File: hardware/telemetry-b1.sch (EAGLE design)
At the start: 128 parts, among them IC1 COPERNICUSSMD, IC10 TPS70933, IC2 TPS70933, IC4 STM32L073CZT6, IC5 TPS62160, IC6 HX1, IC7 LMP7702, IC9 HIH9131, J1 I2C1, J10 TEMP_BAT, J11 DNP, J12 INSOL, J13 SMA_EDGE, J2 I2C2, J3 SMA_EDGE, J4 USD-SOCKET, J5 BAT, J6 SMA_EDGE, J7 SMA_EDGE, J8 TEMP_GPS, J9 TEMP_HOT, K1 ARE104H, K2 ARE104H, K3 ARE104H, Q1 AO3400A, Q2 AO3400A, Q3 AO3400A, U1 LTC3105, U2 INA219, Y1 32768, Y2 8M

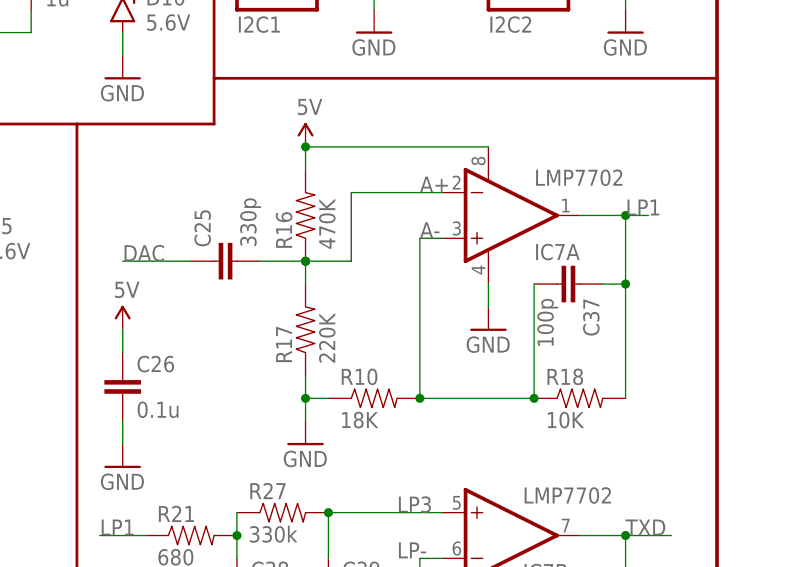
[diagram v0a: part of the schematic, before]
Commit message: Fixed swapped pins in DAC filter
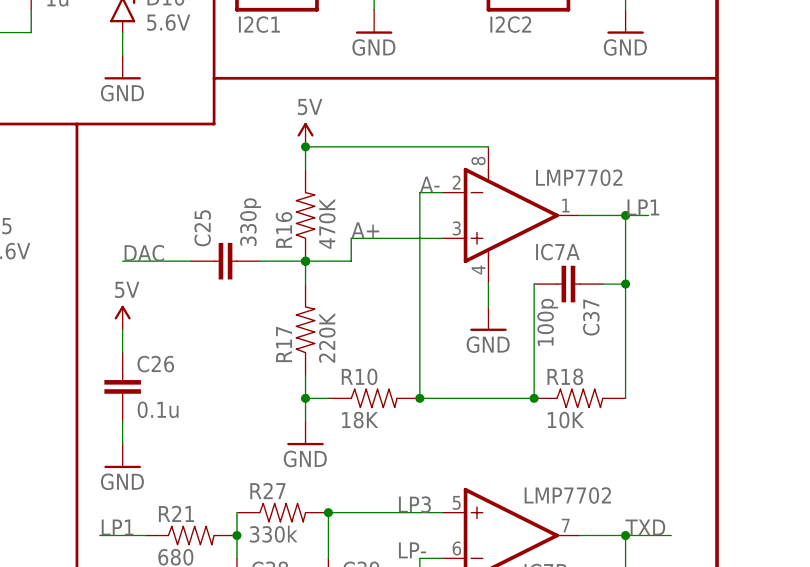
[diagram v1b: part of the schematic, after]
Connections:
- net A+: now also IC7A.+IN; no longer IC7A.-IN
- net A-: now also IC7A.-IN; no longer IC7A.+IN
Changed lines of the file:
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@@
 <net name="A-" class="0">
 <segment>
-<wire x1="215.9" y1="139.7" x2="215.9" y2="121.92" width="0.1524" layer="91"/>
-<label x="215.9" y="139.7" size="1.778" layer="95"/>
-<pinref part="IC7" gate="A" pin="+IN"/>
-<wire x1="218.44" y1="139.7" x2="215.9" y2="139.7" width="0.1524" layer="91"/>
+<wire x1="215.9" y1="144.78" x2="215.9" y2="121.92" width="0.1524" layer="91"/>
 <pinref part="R10" gate="G$1" pin="2"/>
 <pinref part="C37" gate="G$1" pin="2"/>
@@
 <junction x="228.6" y="121.92"/>
 <junction x="215.9" y="121.92"/>
+<pinref part="IC7" gate="A" pin="-IN"/>
+<wire x1="215.9" y1="144.78" x2="218.44" y2="144.78" width="0.1524" layer="91"/>
+<label x="215.9" y="144.78" size="1.778" layer="95"/>
 </segment>
 </net>
@@
 <junction x="203.2" y="137.16"/>
 <junction x="203.2" y="137.16"/>
-<label x="215.9" y="144.78" size="1.778" layer="95"/>
-<wire x1="208.28" y1="144.78" x2="208.28" y2="137.16" width="0.1524" layer="91"/>
+<wire x1="208.28" y1="139.7" x2="208.28" y2="137.16" width="0.1524" layer="91"/>
 <wire x1="208.28" y1="137.16" x2="203.2" y2="137.16" width="0.1524" layer="91"/>
-<pinref part="IC7" gate="A" pin="-IN"/>
-<wire x1="218.44" y1="144.78" x2="208.28" y2="144.78" width="0.1524" layer="91"/>
+<pinref part="IC7" gate="A" pin="+IN"/>
+<wire x1="218.44" y1="139.7" x2="208.28" y2="139.7" width="0.1524" layer="91"/>
+<label x="208.28" y="139.7" size="1.778" layer="95"/>
 </segment>
 </net>

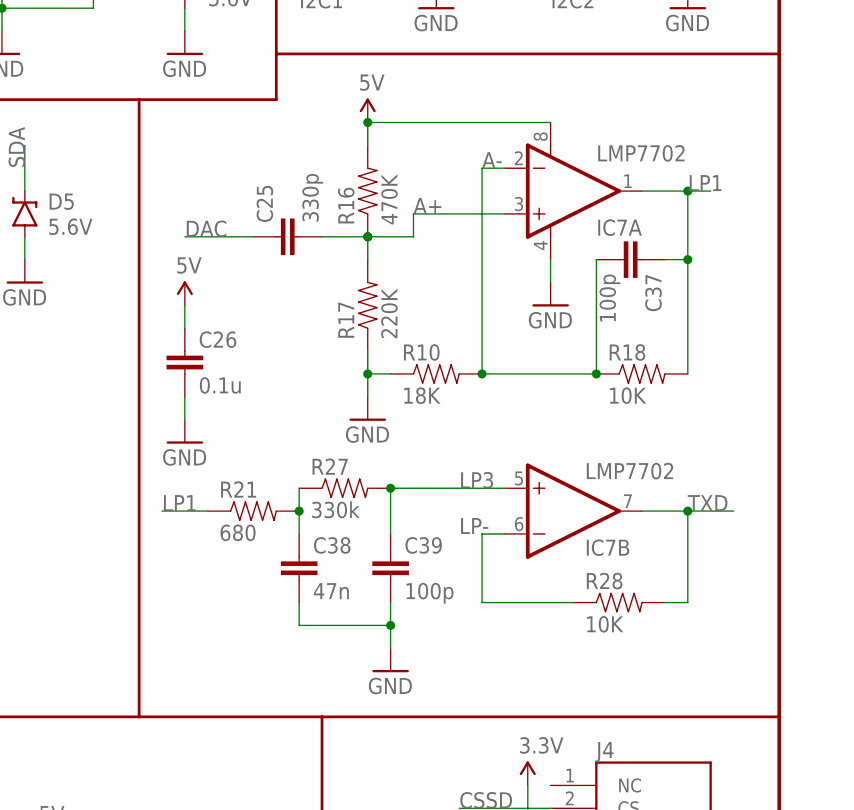
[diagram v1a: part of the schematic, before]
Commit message: Copy filter changes from main Telemetry PCB. Needs a relay rework.
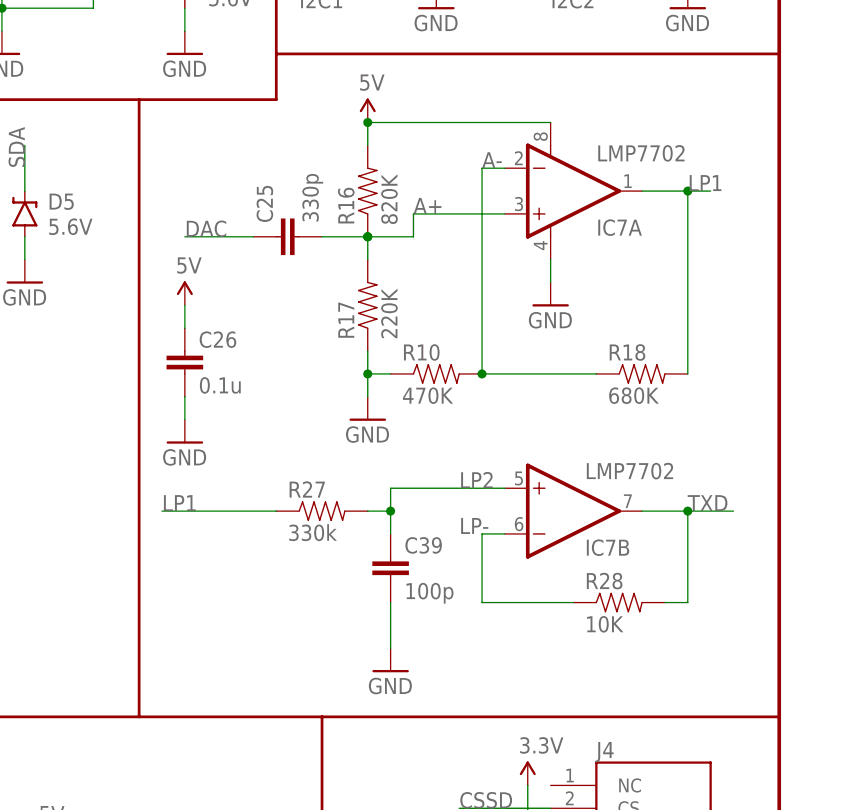
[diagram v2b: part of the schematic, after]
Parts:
- removed C37: 100p, SparkFun-Passives:CAP0805
- removed C38: 47n, SparkFun-Passives:CAP0805
- removed R21: 680, SparkFun-Passives:RESISTOR0805-RES
- R10: value 18K -> 470K
- R16: value 470K -> 820K
- R18: value 10K -> 680K
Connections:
- removed net LP3: C39.1, IC7B.+IN, R27.2
- net A-: no longer C37.2
- net GND: no longer C38.2
- net LP1: now also R27.1; no longer C37.1, R21.1
- net LP2: now also C39.1, IC7B.+IN, R27.2; no longer C38.1, R21.2, R27.1
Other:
- moved on the sheet: R27
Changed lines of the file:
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@@
 <part name="GND25" library="SparkFun-Aesthetics" deviceset="GND" device=""/>
 <part name="C25" library="SparkFun-Passives" deviceset="CAP" device="0805" value="330p"/>
-<part name="R16" library="SparkFun-Passives" deviceset="RESISTOR" device="0805-RES" value="470K"/>
+<part name="R16" library="SparkFun-Passives" deviceset="RESISTOR" device="0805-RES" value="820K"/>
 <part name="R17" library="SparkFun-Passives" deviceset="RESISTOR" device="0805-RES" value="220K"/>
-<part name="R18" library="SparkFun-Passives" deviceset="RESISTOR" device="0805-RES" value="10K"/>
+<part name="R18" library="SparkFun-Passives" deviceset="RESISTOR" device="0805-RES" value="680K"/>
 <part name="C26" library="SparkFun-Passives" deviceset="CAP" device="0805" value="0.1u"/>
 <part name="GND26" library="SparkFun-Aesthetics" deviceset="GND" device=""/>
@@
 <part name="GND48" library="SparkFun-Aesthetics" deviceset="GND" device=""/>
 <part name="SUPPLY20" library="SparkFun-Aesthetics" deviceset="3.3V" device=""/>
-<part name="C37" library="SparkFun-Passives" deviceset="CAP" device="0805" value="100p"/>
-<part name="R10" library="SparkFun-Passives" deviceset="RESISTOR" device="0805-RES" value="18K"/>
-<part name="R21" library="SparkFun-Passives" deviceset="RESISTOR" device="0805-RES" value="680"/>
-<part name="C38" library="SparkFun-Passives" deviceset="CAP" device="0805" value="47n"/>
+<part name="R10" library="SparkFun-Passives" deviceset="RESISTOR" device="0805-RES" value="470K"/>
 <part name="SUPPLY25" library="SparkFun-Aesthetics" deviceset="5V" device=""/>
 <part name="R27" library="SparkFun-Passives" deviceset="RESISTOR" device="0805-RES" value="330k"/>
@@
 <instance part="GND48" gate="1" x="182.88" y="157.48"/>
 <instance part="SUPPLY20" gate="G$1" x="182.88" y="170.18"/>
-<instance part="C37" gate="G$1" x="231.14" y="134.62" rot="R270"/>
 <instance part="R10" gate="G$1" x="210.82" y="121.92"/>
-<instance part="R21" gate="G$1" x="190.5" y="106.68"/>
-<instance part="C38" gate="G$1" x="195.58" y="99.06"/>
 <instance part="SUPPLY25" gate="G$1" x="182.88" y="129.54"/>
-<instance part="R27" gate="G$1" x="200.66" y="109.22"/>
+<instance part="R27" gate="G$1" x="198.12" y="106.68"/>
 <instance part="C39" gate="G$1" x="205.74" y="99.06"/>
 <instance part="R28" gate="G$1" x="231.14" y="96.52"/>
@@
 <segment>
 <pinref part="GND27" gate="1" pin="GND"/>
-<pinref part="C38" gate="G$1" pin="2"/>
-<wire x1="195.58" y1="96.52" x2="195.58" y2="93.98" width="0.1524" layer="91"/>
-<wire x1="195.58" y1="93.98" x2="205.74" y2="93.98" width="0.1524" layer="91"/>
 <pinref part="C39" gate="G$1" pin="2"/>
-<wire x1="205.74" y1="93.98" x2="205.74" y2="91.44" width="0.1524" layer="91"/>
-<wire x1="205.74" y1="96.52" x2="205.74" y2="93.98" width="0.1524" layer="91"/>
-<junction x="205.74" y="93.98"/>
+<wire x1="205.74" y1="96.52" x2="205.74" y2="91.44" width="0.1524" layer="91"/>
 </segment>
 <segment>
@@
 <wire x1="215.9" y1="144.78" x2="215.9" y2="121.92" width="0.1524" layer="91"/>
 <pinref part="R10" gate="G$1" pin="2"/>
-<pinref part="C37" gate="G$1" pin="2"/>
 <pinref part="R18" gate="G$1" pin="1"/>
-<wire x1="228.6" y1="134.62" x2="228.6" y2="121.92" width="0.1524" layer="91"/>
 <wire x1="228.6" y1="121.92" x2="215.9" y2="121.92" width="0.1524" layer="91"/>
-<junction x="228.6" y="121.92"/>
 <junction x="215.9" y="121.92"/>
 <pinref part="IC7" gate="A" pin="-IN"/>
@@
 <net name="LP1" class="0">
 <segment>
-<wire x1="238.76" y1="121.92" x2="238.76" y2="134.62" width="0.1524" layer="91"/>
-<wire x1="238.76" y1="134.62" x2="238.76" y2="142.24" width="0.1524" layer="91"/>
+<wire x1="238.76" y1="121.92" x2="238.76" y2="142.24" width="0.1524" layer="91"/>
 <wire x1="241.3" y1="142.24" x2="238.76" y2="142.24" width="0.1524" layer="91"/>
 <label x="238.76" y="142.24" size="1.778" layer="95"/>
@@
 <junction x="238.76" y="142.24"/>
 <pinref part="R18" gate="G$1" pin="2"/>
-<pinref part="C37" gate="G$1" pin="1"/>
-<wire x1="236.22" y1="134.62" x2="238.76" y2="134.62" width="0.1524" layer="91"/>
-<junction x="238.76" y="134.62"/>
-</segment>
-<segment>
-<pinref part="R21" gate="G$1" pin="1"/>
-<wire x1="180.34" y1="106.68" x2="185.42" y2="106.68" width="0.1524" layer="91"/>
+</segment>
+<segment>
 <label x="180.34" y="106.68" size="1.778" layer="95"/>
+<pinref part="R27" gate="G$1" pin="1"/>
+<wire x1="180.34" y1="106.68" x2="193.04" y2="106.68" width="0.1524" layer="91"/>
 </segment>
 </net>
 <net name="LP2" class="0">
 <segment>
-<pinref part="C38" gate="G$1" pin="1"/>
-<pinref part="R21" gate="G$1" pin="2"/>
-<wire x1="195.58" y1="104.14" x2="195.58" y2="106.68" width="0.1524" layer="91"/>
-<pinref part="R27" gate="G$1" pin="1"/>
-<wire x1="195.58" y1="109.22" x2="195.58" y2="106.68" width="0.1524" layer="91"/>
-<junction x="195.58" y="106.68"/>
-</segment>
-</net>
-<net name="LP3" class="0">
-<segment>
-<pinref part="R27" gate="G$1" pin="2"/>
 <label x="213.36" y="109.22" size="1.778" layer="95"/>
-<pinref part="C39" gate="G$1" pin="1"/>
-<wire x1="205.74" y1="104.14" x2="205.74" y2="109.22" width="0.1524" layer="91"/>
 <pinref part="IC7" gate="B" pin="+IN"/>
 <wire x1="218.44" y1="109.22" x2="205.74" y2="109.22" width="0.1524" layer="91"/>
-<junction x="205.74" y="109.22"/>
-</segment>
-</net>
+<pinref part="C39" gate="G$1" pin="1"/>
+<wire x1="205.74" y1="104.14" x2="205.74" y2="106.68" width="0.1524" layer="91"/>
+<pinref part="R27" gate="G$1" pin="2"/>
+<wire x1="205.74" y1="106.68" x2="205.74" y2="109.22" width="0.1524" layer="91"/>
+<wire x1="205.74" y1="106.68" x2="203.2" y2="106.68" width="0.1524" layer="91"/>
+<junction x="205.74" y="106.68"/>
+</segment>
+</net>

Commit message: Strip unnecessary relay, and fix most RF stubs
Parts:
- removed C10: 0.1u, SparkFun-Passives:CAP0805
- removed D9: BAT20J, SparkFun-DiscreteSemi:DIODE-SCHOTTKY-BAT20J
- removed K3: ARE104H, HAB:RF_RELAY
- removed Q3: AO3400A, SparkFun-DiscreteSemi:MOSFET-NCHANNELAO3404A
- removed R22: 10K, SparkFun-Passives:RESISTOR0805-RES
- removed R29: 180K, SparkFun-Passives:RESISTOR0805-RES
- R30, R31, R32, R33: device SparkFun-Passives:RESISTOR1206 -> SparkFun-Passives:RESISTOR0805-RES
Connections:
- removed net N$3: Q3.G, R22.2, R29.2
- removed net RD2: D9.A, K3G$1.2, Q3.D
- removed net RS2: IC4.PB12, R22.1
- new net RF_STUB: K1G$2.P, K2G$2.O
- net 3.3V: no longer C10.1
- net 5V: no longer D9.C, K3G$1.1
- net GND: no longer C10.2, Q3.S, R29.1
- net RF2: now also K1G$2.O; no longer K3G$2.S
- net RF_HX1: no longer K1G$2.P, K3G$2.P
- net RGND: no longer K3G$2.GND

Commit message: Work on beta PCB layout. Most placement is done, probably will have no room for the HIH (or put it on the back).
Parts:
- renumbered R10 to R29
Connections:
- net N$1 renamed Q2B
- net N$2 renamed Q1B
- net N$4 renamed BVOUT
- net CSSD: now also IC4.PB7; no longer IC4.PA15
- net RS0: now also IC4.PB14; no longer IC4.PB7
- net RS1: now also IC4.PB15; no longer IC4.PB6
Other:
- moved on the sheet: R26, R6
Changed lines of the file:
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@@
 <part name="GND48" library="SparkFun-Aesthetics" deviceset="GND" device=""/>
 <part name="SUPPLY20" library="SparkFun-Aesthetics" deviceset="3.3V" device=""/>
-<part name="R10" library="SparkFun-Passives" deviceset="RESISTOR" device="0805-RES" value="470K"/>
+<part name="R29" library="SparkFun-Passives" deviceset="RESISTOR" device="0805-RES" value="470K"/>
 <part name="SUPPLY25" library="SparkFun-Aesthetics" deviceset="5V" device=""/>
 <part name="R27" library="SparkFun-Passives" deviceset="RESISTOR" device="0805-RES" value="330k"/>
@@
 <instance part="SUPPLY8" gate="G$1" x="88.9" y="177.8"/>
 <instance part="SUPPLY9" gate="G$1" x="12.7" y="167.64"/>
-<instance part="SUPPLY11" gate="G$1" x="73.66" y="111.76"/>
+<instance part="SUPPLY11" gate="G$1" x="71.12" y="111.76"/>
 <instance part="Y1" gate="G$1" x="45.72" y="124.46" smashed="yes">
 <attribute name="NAME" x="44.196" y="127" size="1.778" layer="95"/>
@@
 <instance part="C36" gate="G$1" x="162.56" y="167.64"/>
 <instance part="GND44" gate="1" x="162.56" y="157.48"/>
-<instance part="R6" gate="G$1" x="73.66" y="104.14" rot="R90"/>
-<instance part="R26" gate="G$1" x="66.04" y="104.14" rot="R90"/>
+<instance part="R6" gate="G$1" x="71.12" y="104.14" rot="R90"/>
+<instance part="R26" gate="G$1" x="63.5" y="104.14" rot="R90"/>
 <instance part="R24" gate="G$1" x="101.6" y="137.16" rot="R180"/>
 <instance part="SUPPLY15" gate="G$1" x="109.22" y="149.86"/>
@@
 <instance part="GND48" gate="1" x="182.88" y="157.48"/>
 <instance part="SUPPLY20" gate="G$1" x="182.88" y="170.18"/>
-<instance part="R10" gate="G$1" x="210.82" y="121.92"/>
+<instance part="R29" gate="G$1" x="210.82" y="121.92"/>
 <instance part="SUPPLY25" gate="G$1" x="182.88" y="129.54"/>
 <instance part="R27" gate="G$1" x="198.12" y="106.68"/>
@@
 <pinref part="R17" gate="G$1" pin="1"/>
 <wire x1="203.2" y1="119.38" x2="203.2" y2="121.92" width="0.1524" layer="91"/>
-<pinref part="R10" gate="G$1" pin="1"/>
+<pinref part="R29" gate="G$1" pin="1"/>
 <wire x1="203.2" y1="121.92" x2="203.2" y2="124.46" width="0.1524" layer="91"/>
 <wire x1="205.74" y1="121.92" x2="203.2" y2="121.92" width="0.1524" layer="91"/>
@@
 <segment>
 <pinref part="SUPPLY11" gate="G$1" pin="3.3V"/>
-<wire x1="73.66" y1="111.76" x2="73.66" y2="109.22" width="0.1524" layer="91"/>
-<wire x1="73.66" y1="109.22" x2="66.04" y2="109.22" width="0.1524" layer="91"/>
+<wire x1="71.12" y1="111.76" x2="71.12" y2="109.22" width="0.1524" layer="91"/>
+<wire x1="71.12" y1="109.22" x2="63.5" y2="109.22" width="0.1524" layer="91"/>
 <pinref part="R6" gate="G$1" pin="2"/>
-<junction x="73.66" y="109.22"/>
+<junction x="71.12" y="109.22"/>
 <pinref part="R26" gate="G$1" pin="2"/>
 </segment>
@@
 <net name="OSC32_IN" class="0">
 <segment>
+<pinref part="IC4" gate="G$1" pin="OSC32_IN"/>
+<wire x1="30.48" y1="73.66" x2="45.72" y2="73.66" width="0.1524" layer="91"/>
+<label x="30.48" y="73.66" size="1.778" layer="95"/>
+</segment>
+<segment>
 <pinref part="C8" gate="G$1" pin="1"/>
 <wire x1="43.18" y1="124.46" x2="38.1" y2="124.46" width="0.1524" layer="91"/>
@@
 <pinref part="Y1" gate="G$1" pin="1"/>
 </segment>
-<segment>
-<pinref part="IC4" gate="G$1" pin="OSC32_IN"/>
-<wire x1="30.48" y1="73.66" x2="45.72" y2="73.66" width="0.1524" layer="91"/>
-<label x="30.48" y="73.66" size="1.778" layer="95"/>
-</segment>
 </net>
 <net name="OSC32_OUT" class="0">
+<segment>
+<pinref part="IC4" gate="G$1" pin="OSC32_OUT"/>
+<wire x1="30.48" y1="71.12" x2="45.72" y2="71.12" width="0.1524" layer="91"/>
+<label x="30.48" y="71.12" size="1.778" layer="95"/>
+</segment>
 <segment>
 <pinref part="C9" gate="G$1" pin="1"/>
@@
 <pinref part="Y1" gate="G$1" pin="2"/>
 </segment>
-<segment>
-<pinref part="IC4" gate="G$1" pin="OSC32_OUT"/>
-<wire x1="30.48" y1="71.12" x2="45.72" y2="71.12" width="0.1524" layer="91"/>
-<label x="30.48" y="71.12" size="1.778" layer="95"/>
-</segment>
 </net>
 <net name="OSC_OUT" class="0">
@@
 <pinref part="IC4" gate="G$1" pin="BOOT0"/>
 <label x="63.5" y="88.9" size="1.778" layer="95" rot="R90"/>
-<wire x1="63.5" y1="86.36" x2="63.5" y2="96.52" width="0.1524" layer="91"/>
-<wire x1="63.5" y1="96.52" x2="66.04" y2="96.52" width="0.1524" layer="91"/>
-<wire x1="66.04" y1="96.52" x2="66.04" y2="99.06" width="0.1524" layer="91"/>
+<wire x1="63.5" y1="86.36" x2="63.5" y2="99.06" width="0.1524" layer="91"/>
 <pinref part="R26" gate="G$1" pin="1"/>
 </segment>
@@
 <net name="RS0" class="0">
 <segment>
-<pinref part="IC4" gate="G$1" pin="PB7"/>
-<label x="66.04" y="88.9" size="1.778" layer="95" rot="R90"/>
-<wire x1="66.04" y1="86.36" x2="66.04" y2="91.44" width="0.1524" layer="91"/>
-</segment>
-<segment>
 <pinref part="R3" gate="G$1" pin="1"/>
 <wire x1="429.26" y1="152.4" x2="434.34" y2="152.4" width="0.1524" layer="91"/>
 <label x="429.26" y="152.4" size="1.778" layer="95"/>
 </segment>
+<segment>
+<pinref part="IC4" gate="G$1" pin="PB14"/>
+<wire x1="101.6" y1="55.88" x2="96.52" y2="55.88" width="0.1524" layer="91"/>
+<label x="99.06" y="55.88" size="1.778" layer="95"/>
+</segment>
 </net>
 <net name="RS1" class="0">
-<segment>
-<pinref part="IC4" gate="G$1" pin="PB6"/>
-<label x="68.58" y="88.9" size="1.778" layer="95" rot="R90"/>
-<wire x1="68.58" y1="86.36" x2="68.58" y2="91.44" width="0.1524" layer="91"/>
-</segment>
 <segment>
 <pinref part="R8" gate="G$1" pin="1"/>
 <wire x1="408.94" y1="104.14" x2="414.02" y2="104.14" width="0.1524" layer="91"/>
 <label x="408.94" y="104.14" size="1.778" layer="95"/>
+</segment>
+<segment>
+<pinref part="IC4" gate="G$1" pin="PB15"/>
+<wire x1="101.6" y1="58.42" x2="96.52" y2="58.42" width="0.1524" layer="91"/>
+<label x="99.06" y="58.42" size="1.778" layer="95"/>
 </segment>
 </net>
@@
 </segment>
 <segment>
-<pinref part="IC4" gate="G$1" pin="PA15"/>
-<label x="78.74" y="88.9" size="1.778" layer="95" rot="R90"/>
-<wire x1="78.74" y1="86.36" x2="78.74" y2="96.52" width="0.1524" layer="91"/>
-<wire x1="78.74" y1="96.52" x2="73.66" y2="96.52" width="0.1524" layer="91"/>
-<wire x1="73.66" y1="96.52" x2="73.66" y2="99.06" width="0.1524" layer="91"/>
+<wire x1="71.12" y1="96.52" x2="71.12" y2="99.06" width="0.1524" layer="91"/>
 <pinref part="R6" gate="G$1" pin="1"/>
+<wire x1="71.12" y1="96.52" x2="66.04" y2="96.52" width="0.1524" layer="91"/>
+<pinref part="IC4" gate="G$1" pin="PB7"/>
+<label x="66.04" y="88.9" size="1.778" layer="95" rot="R90"/>
+<wire x1="66.04" y1="86.36" x2="66.04" y2="96.52" width="0.1524" layer="91"/>
 </segment>
 </net>
@@
 <segment>
 <wire x1="215.9" y1="144.78" x2="215.9" y2="121.92" width="0.1524" layer="91"/>
-<pinref part="R10" gate="G$1" pin="2"/>
+<pinref part="R29" gate="G$1" pin="2"/>
 <pinref part="R18" gate="G$1" pin="1"/>
 <wire x1="228.6" y1="121.92" x2="215.9" y2="121.92" width="0.1524" layer="91"/>
@@
 </segment>
 </net>
-<net name="N$2" class="0">
+<net name="Q1B" class="0">
 <segment>
 <pinref part="R3" gate="G$1" pin="2"/>
@@
 <wire x1="447.04" y1="149.86" x2="447.04" y2="152.4" width="0.1524" layer="91"/>
 <junction x="447.04" y="152.4"/>
+<label x="444.5" y="152.4" size="1.778" layer="95"/>
 </segment>
 </net>
@@
 </segment>
 </net>
-<net name="N$1" class="0">
+<net name="Q2B" class="0">
 <segment>
 <pinref part="R8" gate="G$1" pin="2"/>
@@
 <wire x1="426.72" y1="101.6" x2="426.72" y2="104.14" width="0.1524" layer="91"/>
 <junction x="426.72" y="104.14"/>
+<label x="424.18" y="104.14" size="1.778" layer="95"/>
 </segment>
 </net>
@@
 </segment>
 </net>
-<net name="N$4" class="0">
+<net name="BVOUT" class="0">
 <segment>
 <pinref part="U2" gate="G$1" pin="IN-"/>
@@
 <junction x="309.88" y="91.44"/>
 <pinref part="JP4" gate="G$1" pin="2"/>
-</segment>
-</net>
+<label x="299.72" y="91.44" size="1.778" layer="95"/>
+</segment>
+</net>
